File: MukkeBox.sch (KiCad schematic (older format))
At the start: 7 parts

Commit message: BMS fertig, Charger fertig, Amplifier fertig. TODO: Charge vs Discharge LiPo wie machen sachen
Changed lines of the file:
@@
 $Descr A4 11693 8268
 encoding utf-8
-Sheet 1 4
+Sheet 1 5
 Title ""
 Date ""
@@
 L Connector:Conn_ARM_JTAG_SWD_10 J
 U 1 1 5E6D4F79
-P 1850 1300
-F 0 "J" H 1410 1346 50  0000 R CNN
-F 1 "Conn_ARM_JTAG_SWD_10" H 1410 1255 50  0000 R CNN
-F 2 "Connector_PinHeader_1.27mm:PinHeader_2x05_P1.27mm_Vertical_SMD" H 1900 750 50  0001 L TNN
-F 3 "" V 1500 50  50  0001 C CNN
-	1    1850 1300
+P 1550 3000
+F 0 "J" H 1110 3046 50  0000 R CNN
+F 1 "Conn_ARM_JTAG_SWD_10" H 1110 2955 50  0000 R CNN
+F 2 "Connector_PinHeader_1.27mm:PinHeader_2x05_P1.27mm_Vertical_SMD" H 1600 2450 50  0001 L TNN
+F 3 "" V 1200 1750 50  0001 C CNN
+	1    1550 3000
 	1    0    0    -1
 $EndComp
@@
 	2750 3300 2750 3450
 $Sheet
-S 5300 800  1200 1050
+S 2350 750  1050 1050
 U 5E73BADE
-F0 "02_BMS" 50
-F1 "02_BMS.sch" 50
-$EndSheet
-$Sheet
-S 2700 800  1100 1050
+F0 "01_BMS" 50
+F1 "01_BMS.sch" 50
+$EndSheet
+$Sheet
+S 3900 750  1100 1050
 U 5E73BAE8
-F0 "00_StepUp" 50
-F1 "00_StepUp.sch" 50
-$EndSheet
-$Sheet
-S 4000 800  1050 1050
+F0 "02_StepUp" 50
+F1 "02_StepUp.sch" 50
+$EndSheet
+$Sheet
+S 800  750  1050 1050
 U 5E73BB4A
-F0 "01_Charger" 50
-F1 "01_Charger.sch" 50
+F0 "00_Charger" 50
+F1 "00_Charger.sch" 50
+$EndSheet
+$Sheet
+S 7900 800  1150 950
+U 5E751A81
+F0 "Amplifier" 50
+F1 "Amplifier.sch" 50
 $EndSheet
 $EndSCHEMATC

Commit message: LDO für Audio DSP hinzugefügt
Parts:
- removed U: TDA7418, symbol MySymbols:TDA7418
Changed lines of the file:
@@
 $Descr A4 11693 8268
 encoding utf-8
-Sheet 1 5
+Sheet 1 6
 Title ""
 Date ""
@@
 $EndDescr
 $Comp
-L MySymbols:TDA7418 U
-U 1 1 5E6D49E0
-P 9900 3600
-F 0 "U" H 10150 4550 50  0000 C CNN
-F 1 "TDA7418" H 9900 3650 50  0000 C CNN
-F 2 "" H 9700 3650 50  0001 C CNN
-F 3 "" H 9700 3650 50  0001 C CNN
-	1    9900 3600
-	1    0    0    -1
-$EndComp
-$Comp
 L Audio:PCM5100 U
 U 1 1 5E6DC9C9
@@
 F1 "Amplifier.sch" 50
 $EndSheet
+$Sheet
+S 6800 800  1000 950
+U 5EA6895E
+F0 "AudioProcessor" 50
+F1 "AudioProcessor.sch" 50
+$EndSheet
 $EndSCHEMATC

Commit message: 3v3 über LDO von BMS enablen. Bluetooth hinzugefügt
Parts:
- removed J: Conn_ARM_JTAG_SWD_10, Connector_PinHeader_1.27mm:PinHeader_2x05_P1.27mm_Vertical_SMD, symbol Connector:Conn_ARM_JTAG_SWD_10
- removed R?: 10k, symbol Device:R
- removed R?: 47k, symbol Device:R
- removed U: PCM5100, Package_SO:TSSOP-20_4.4x6.5mm_P0.65mm, symbol Audio:PCM5100
- removed U: STM32F410C8Ux, Package_DFN_QFN:QFN-48-1EP_7x7mm_P0.5mm_EP5.6x5.6mm, symbol MCU_ST_STM32F4:STM32F410CBUx
- added C102, C103, C104, C105: 100n, symbol Device:C
- added C?: 1uF 36V, symbol Device:C_Small
- added C?: 1uF, symbol Device:C_Small
- added C?: 100nF, symbol Device:C_Small
- added D101: LED_25%, symbol Device:LED
- added D102: LED_50%, symbol Device:LED
- added D103: LED_75%, symbol Device:LED
- added D104: LED_100%, symbol Device:LED
- added J101: ST_Link_V2_10P, symbol Connector:ST_Link_V2_10P
- added R101, R102, R103, R104: 100R, symbol Device:R_Small
- added SW?: SW_DIP_x01, symbol Switch:SW_DIP_x01
- added U101: STM32F030C8Tx, Package_QFP:LQFP-48_7x7mm_P0.5mm, symbol MCU_ST_STM32F0:STM32F030C8Tx
- added U?: TPS7B82-Q1, symbol Regulator_Linear:TPS7B82-Q1
- gave numbers to parts that had none: 1
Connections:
- net labels added: ALERT_BQ76920, AUX_DETECT, Akku_100%, Akku_25%, Akku_50%, Akku_75%, BATTERY+, BOOT_BQ76920, CELL1_SENSE, CHARGER_DISABLE, CHARGER_IOUT, DIAG_TDA, ENABLE_9V, LDO_BQ76920, MUTE_TDA7418, MUTE_TDA7498L, RxD, SCL, SDA, STBY_TDA7498L, TxD
- wire segments 28 -> 45
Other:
- note added: "Akkuanzeige"
- note added: "Charging Current\n (max. 4V entspricht 200mV Shunt)"
- note added: "GPIO"
- note added: "Helligkeit prüfen."
- note added: "Startet das Batterie Management System"
- note added: "Vom Batterie Management System\nLDO wecken lassen"
- note removed: "32Bit I2S Audio DAC\n"
- note removed: "Audio Digitial Signal Processor\n"

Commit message: power schalter und taser hinzugefügt. Selbsthaltung LDO hinzugefügt. Gain Potis hinzugefügt, Separater Ground für Audio Lines
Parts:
- removed C101, C102, C103, C104, C105: 100n, symbol Device:C
- added C? (x8): 100nF, symbol Device:C_Small
- added D? (x2): D_Small, symbol Device:D_Small
- added Q?: Q_NPN_CBE, symbol Device:Q_NPN_CBE
- added R? (x14): 10K, symbol Device:R_Small
- added R?: 100K, symbol Device:R_Small
- added RV? (x4): 100K, symbol Device:R_POT
- added SW?: PLAY, symbol Switch:SW_MEC_5G
- added SW?: MUTE, symbol Switch:SW_MEC_5G
- added SW?: NEXT, symbol Switch:SW_MEC_5G
- added SW?: BACK, symbol Switch:SW_MEC_5G
- added SW?: VOL+, symbol Switch:SW_MEC_5G
- added SW?: VOL-, symbol Switch:SW_MEC_5G
- SW?: value SW_DIP_x01 -> Power
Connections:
- net labels added: BASS, Back, EN_3V3, GAIN, MIDDLE, Mute, Next, POWER_I, POWER_OFF_O, Play, RxT, SWDIO, TREBLE, TxR, Vol+, Vol-
- net labels removed: LDO_BQ76920, RxD, TxD
- wire segments 45 -> 154
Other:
- note added: "ANA_IN"
- note added: "CAPS CPU"
- note added: "GPI"
- note added: "GPI 10x\nGPO 11x\nGPIO 6x\nANA_IN 5x"
- note added: "GPO"
- note added: "Gain Potis"
- note added: "LDO über Controler abschalten"
- note added: "Power Schalter und Taster"
- note added: "Schalter Abfrage"
- note added: "Selbsthaltung"
- moved on the sheet: C?, J101, SW?, U?

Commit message: Schaltplan fertig. Fertig für review
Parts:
- removed Q?: Q_NPN_CBE, symbol Device:Q_NPN_CBE
- removed U101: STM32F030C8Tx, Package_QFP:LQFP-48_7x7mm_P0.5mm, symbol MCU_ST_STM32F0:STM32F030C8Tx
- added J? (x4): Jumper, symbol Connector_Generic:Conn_02x01
- added Q?: NTK3043N, symbol Device:Q_NMOS_GSD
- added R?: 10K, symbol Device:R_Small
- added U?: STM32F030C6Tx_MukkeBox, Package_QFP:LQFP-48_7x7mm_P0.5mm, symbol MCU_ST_STM32F0:STM32F030C6Tx_MukkeBox
- C? (x4): value 100nF -> 10nF
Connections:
- net labels added: CHARGER_PLUGGED, CP_EN, DIAG_TDA7498, MUTE_TDA7498, PACK_VOLTAGE, PCHG_EN, PMON_EN, RST, STBY_TDA7498, SWCLK
- net labels removed: DIAG_TDA, MUTE_TDA7498L, STBY_TDA7498L
- wire segments 154 -> 218
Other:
- note added: "GPI: active low"
- note added: "GPO: active high"
- note added: "GPO: active low"
- note added: "GPO: active low?!"
- note removed: "32Bit MCU \n"
- note removed: "LDO über Controler abschalten"
- moved on the sheet: C?, D?, R?

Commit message: Footprintzuordnung angefangen
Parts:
- added C104, C105: 20pF, Capacitor_SMD:C_0603_1608Metric_Pad1.05x0.95mm_HandSolder, symbol Device:C_Small
- added J106: Jumper, symbol Connector_Generic:Conn_02x01
- added R116: DNP, symbol Device:R_Small
- added R117: 10K, symbol Device:R_Small
- added Y101: FOXSDLF/080-20, symbol Device:Crystal
- C101, C102, C103, C106, C107, C108, C109, C110, C111, C112, C113: renamed from C?; footprint (none) -> Capacitor_SMD:C_0603_1608Metric_Pad1.05x0.95mm_HandSolder
- gave numbers to parts that had none: 36
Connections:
- wire segments 218 -> 235
- no-connect marks 0 -> 3
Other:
- moved on the sheet: C103, C106, C107, C108, C109, R115

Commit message: fast alle footprints herausgesucht. Spulen typen rausgesucht: Bourns spulen
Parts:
- removed SW101: Power, symbol Switch:SW_DIP_x01
- removed SW102: PLAY, symbol Switch:SW_MEC_5G
- removed SW103: MUTE, symbol Switch:SW_MEC_5G
- removed SW104: NEXT, symbol Switch:SW_MEC_5G
- removed SW105: BACK, symbol Switch:SW_MEC_5G
- removed SW106: VOL+, symbol Switch:SW_MEC_5G
- removed SW107: VOL-, symbol Switch:SW_MEC_5G
- added J107: PinHeader, Connector_PinHeader_2.54mm:PinHeader_2x08_P2.54mm_Vertical_SMD, symbol Connector_Generic:Conn_02x08_Odd_Even
- added R123: 10K, Resistor_SMD:R_0603_1608Metric_Pad1.05x0.95mm_HandSolder, symbol Device:R_Small
- D101, D102, D103, D104: footprint (none) -> LED_THT:LED_D5.0mm
- D105, D106: value D_Small -> SS16HE; footprint (none) -> Diode_SMD:D_SOD-323
- J101: footprint (none) -> Connector_PinHeader_2.54mm:PinHeader_2x05_P2.54mm_Vertical
- J102, J103, J104, J105, J106: footprint (none) -> Connector_PinHeader_2.54mm:PinHeader_1x02_P2.54mm_Vertical
- Q101: footprint (none) -> Package_TO_SOT_SMD:SOT-723
- R101, R102, R103, R104: value 100R -> 1K; footprint (none) -> Resistor_SMD:R_0603_1608Metric_Pad1.05x0.95mm_HandSolder
- R105, R106, R107, R108, R109, R110, R111, R112, R113, R114, R115, R116, R117, R118, R119, R120, R121, R122: footprint (none) -> Resistor_SMD:R_0603_1608Metric_Pad1.05x0.95mm_HandSolder
- U101: footprint (none) -> Package_DFN_QFN:Texas_S-PWSON-N6_ThermalVias
- U102: footprint Package_QFP:LQFP-48_7x7mm_P0.5mm -> Package_QFP:LQFP-64_10x10mm_P0.5mm
- Y101: footprint (none) -> Crystal:Crystal_SMD_HC49-SD_HandSoldering
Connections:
- net +3V3: now also R123.2
- net Back: now also J107.9 (Pin_9)
- net CELL1_SENSE: now also J107.1 (Pin_1)
- net GND: now also U101.7 (GND_Term), J107.10 (Pin_10), J107.12 (Pin_12), J107.14 (Pin_14), J107.16 (Pin_16), J107.4 (Pin_4), J107.6 (Pin_6), J107.8 (Pin_8)
- net Mute: now also J107.5 (Pin_5)
- net Next: now also J107.7 (Pin_7)
- net Play: now also J107.3 (Pin_3)
- net at R111.2, R112.2, R113.2: now also J107.2 (Pin_2)
- net AUX_DETECT renamed Res1
- net Res1: now also J107.15 (Pin_15), R123.1
- net Vol+ renamed BT_Pair
- net BT_Pair: now also J107.11 (Pin_11)
- net Vol- renamed AUX_BT
- net AUX_BT: now also J107.13 (Pin_13)
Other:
- moved on the sheet: R106, R107, R108, R109, R110

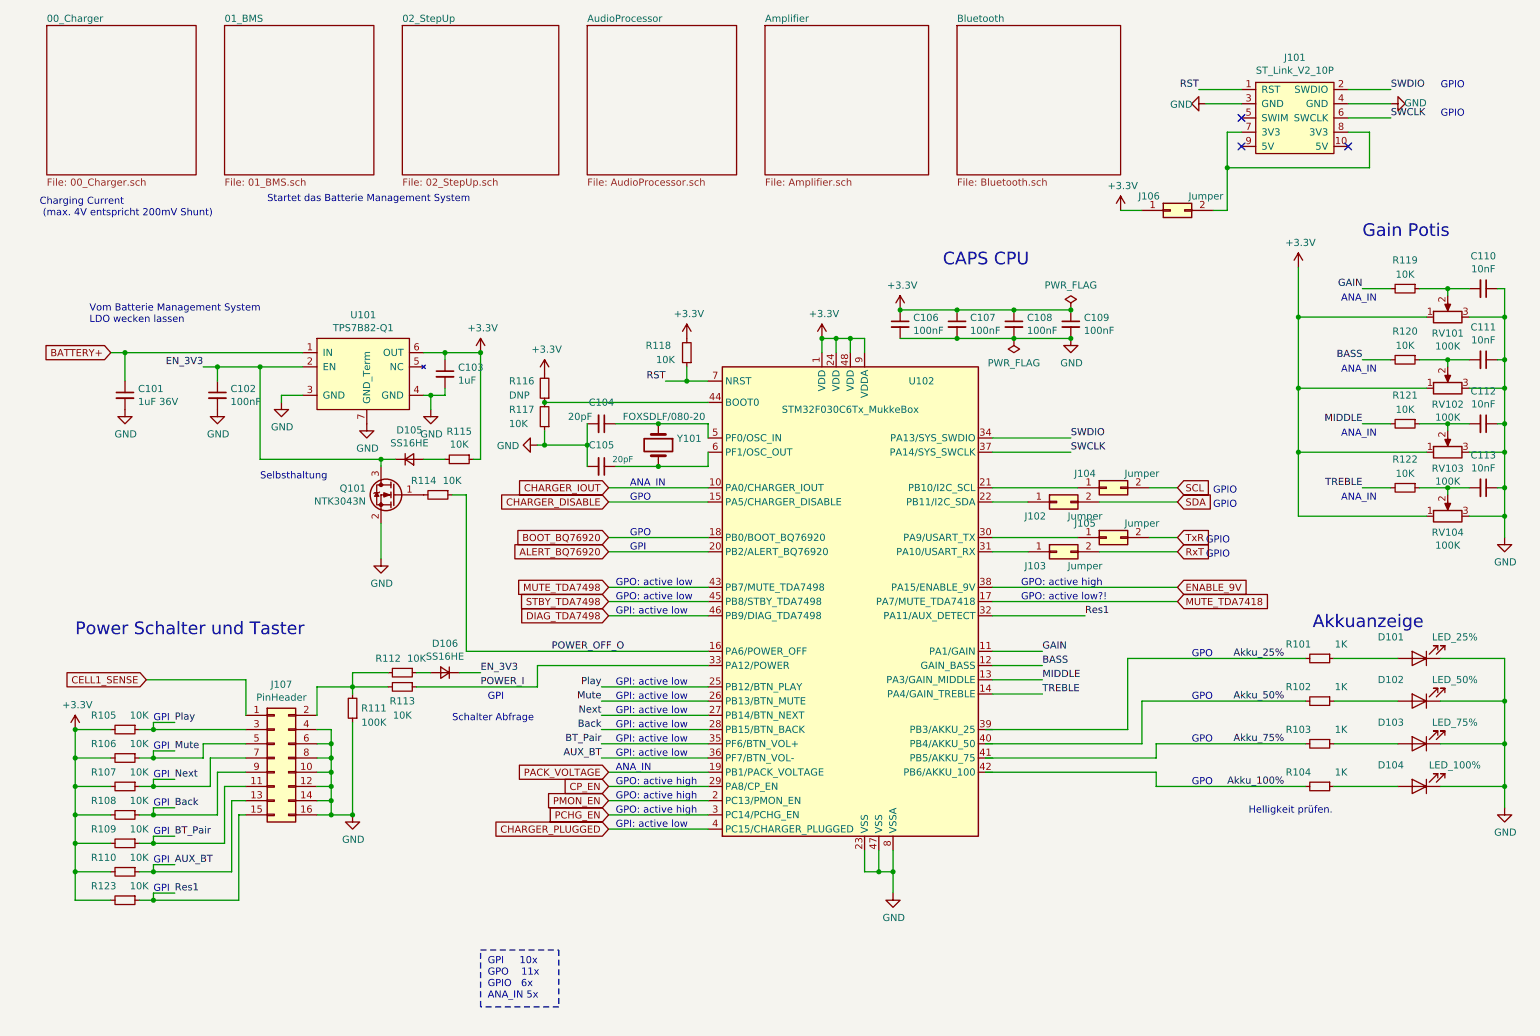
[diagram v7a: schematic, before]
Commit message: Port Expander und Rotary Encoder hinzugefügt. TODO: Footprint Heatsink Amp
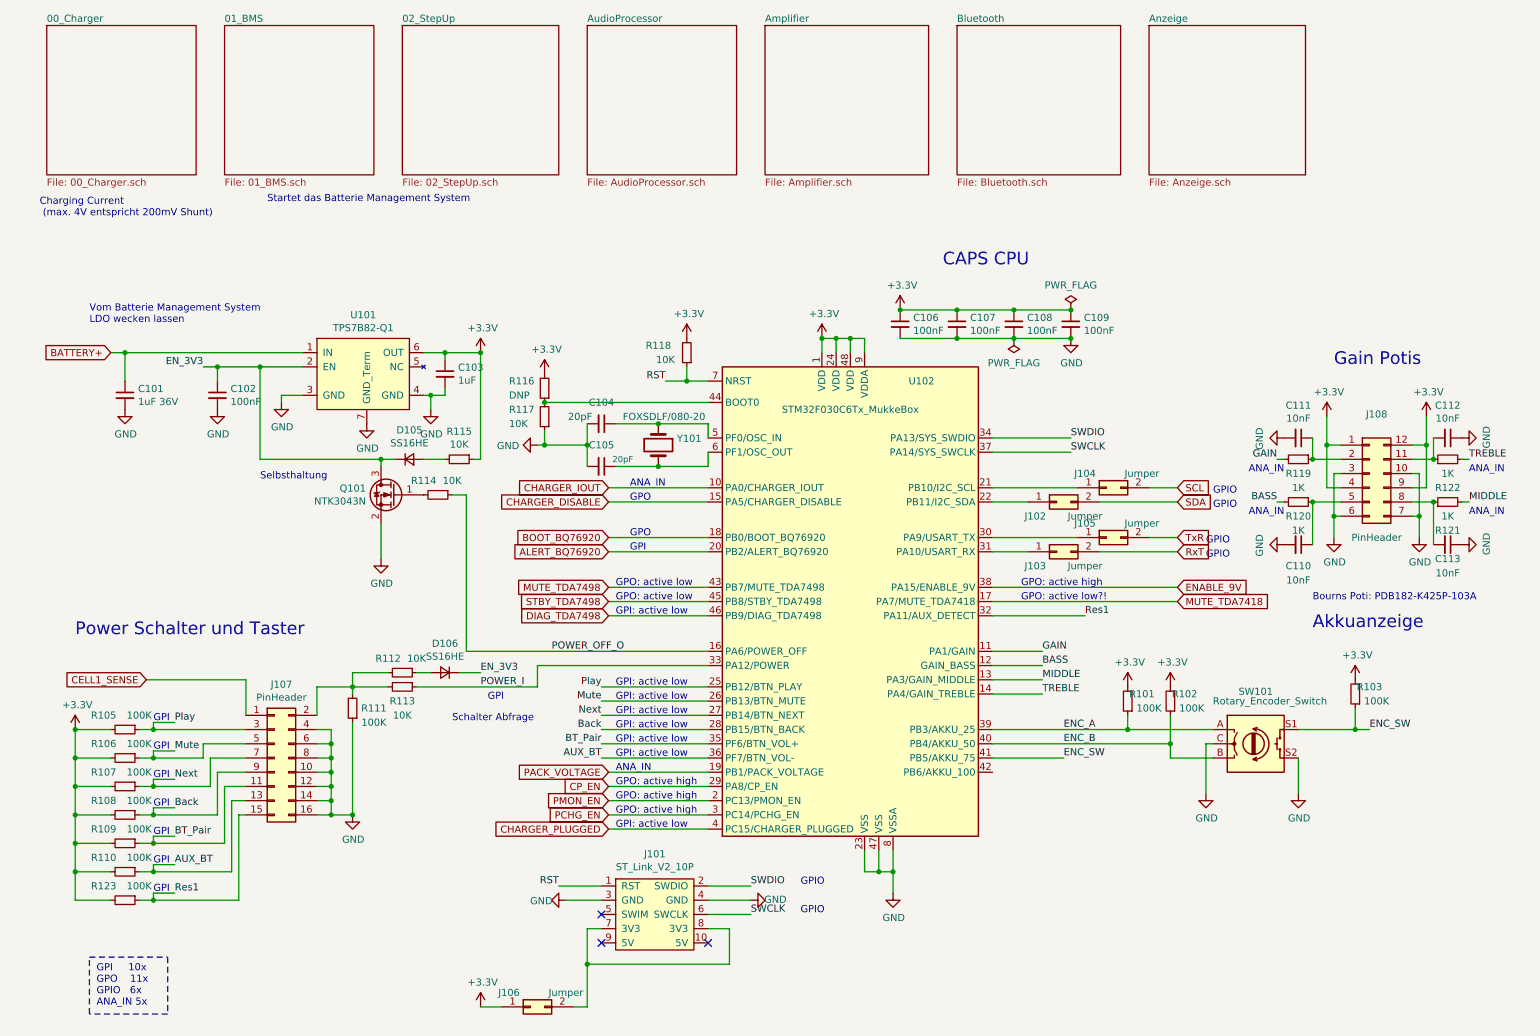
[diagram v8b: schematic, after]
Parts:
- removed D101: LED_25%, LED_THT:LED_D5.0mm, symbol Device:LED
- removed D102: LED_50%, LED_THT:LED_D5.0mm, symbol Device:LED
- removed D103: LED_75%, LED_THT:LED_D5.0mm, symbol Device:LED
- removed D104: LED_100%, LED_THT:LED_D5.0mm, symbol Device:LED
- removed R104: 1K, Resistor_SMD:R_0603_1608Metric_Pad1.05x0.95mm_HandSolder, symbol Device:R_Small
- removed RV101, RV102, RV103, RV104: 100K, symbol Device:R_POT
- added J108: PinHeader, Connector_PinHeader_2.54mm:PinHeader_2x06_P2.54mm_Vertical_SMD, symbol Connector_Generic:Conn_02x06_Counter_Clockwise
- added SW101: Rotary_Encoder_Switch, Rotary_Encoder:RotaryEncoder_Alps_EC11E-Switch_Vertical_H20mm_CircularMountingHoles, symbol Device:Rotary_Encoder_Switch
- R101, R102, R103: value 1K -> 100K
- R105, R106, R107, R108, R109, R110, R123: value 10K -> 100K
- R119, R120, R121, R122: value 10K -> 1K
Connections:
- net Akku_25% is gone; now on net +3V3: R101.2
- net Akku_50% is gone; now on net +3V3: R102.2
- net Akku_75% is gone; now on net +3V3: R103.2
- net +3V3: now also J108.1 (Pin_1), J108.12 (Pin_12), J108.4 (Pin_4), J108.9 (Pin_9)
- net GND: now also C110.2, C111.2, J108.10 (Pin_10), J108.3 (Pin_3), J108.6 (Pin_6), J108.7 (Pin_7), SW101.C, SW101.S2; no longer C110.1, C111.1
- net ENC_A: now reaches R101.1
- net ENC_A: now also U102.39 (PB3/AKKU_25), SW101.A
- net ENC_B: now reaches R102.1
- net ENC_B: now also U102.40 (PB4/AKKU_50), SW101.B
- net ENC_SW: now reaches R103.1
- net ENC_SW: now also U102.41 (PB5/AKKU_75), SW101.S1
- net at R122.1: now also C112.2, J108.11 (Pin_11); no longer C113.2
- net at R121.1: now also C113.2, J108.8 (Pin_8); no longer C112.2
- net at R120.1: now also C110.1, J108.5 (Pin_5); no longer C111.2
- net at R119.1: now also C111.1, J108.2 (Pin_2); no longer C110.2
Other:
- note added: "Bourns Poti: PDB182-K425P-103A"
- note removed: "Helligkeit prüfen."
- moved on the sheet: C110, C111, C112, C113, J101, J106, R119, R120, R121, R122
